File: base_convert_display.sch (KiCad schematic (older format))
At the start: 49 parts, among them Q10 Q_PNP_BEC, Q11 Q_NPN_BEC, Q12 Q_NPN_BEC, Q13 Q_NPN_BEC, Q14 Q_NPN_BEC, Q15 Q_NPN_BEC, Q16 Q_NPN_BEC, Q17 Q_NPN_BEC, Q2 Q_PNP_BEC, Q26 Q_PNP_BEC, Q27 Q_NPN_BEC, Q3 Q_PNP_BEC, Q4 Q_PNP_BEC, Q5 Q_PNP_BEC, Q6 Q_PNP_BEC, Q7 Q_PNP_BEC, Q8 Q_PNP_BEC, Q9 Q_PNP_BEC

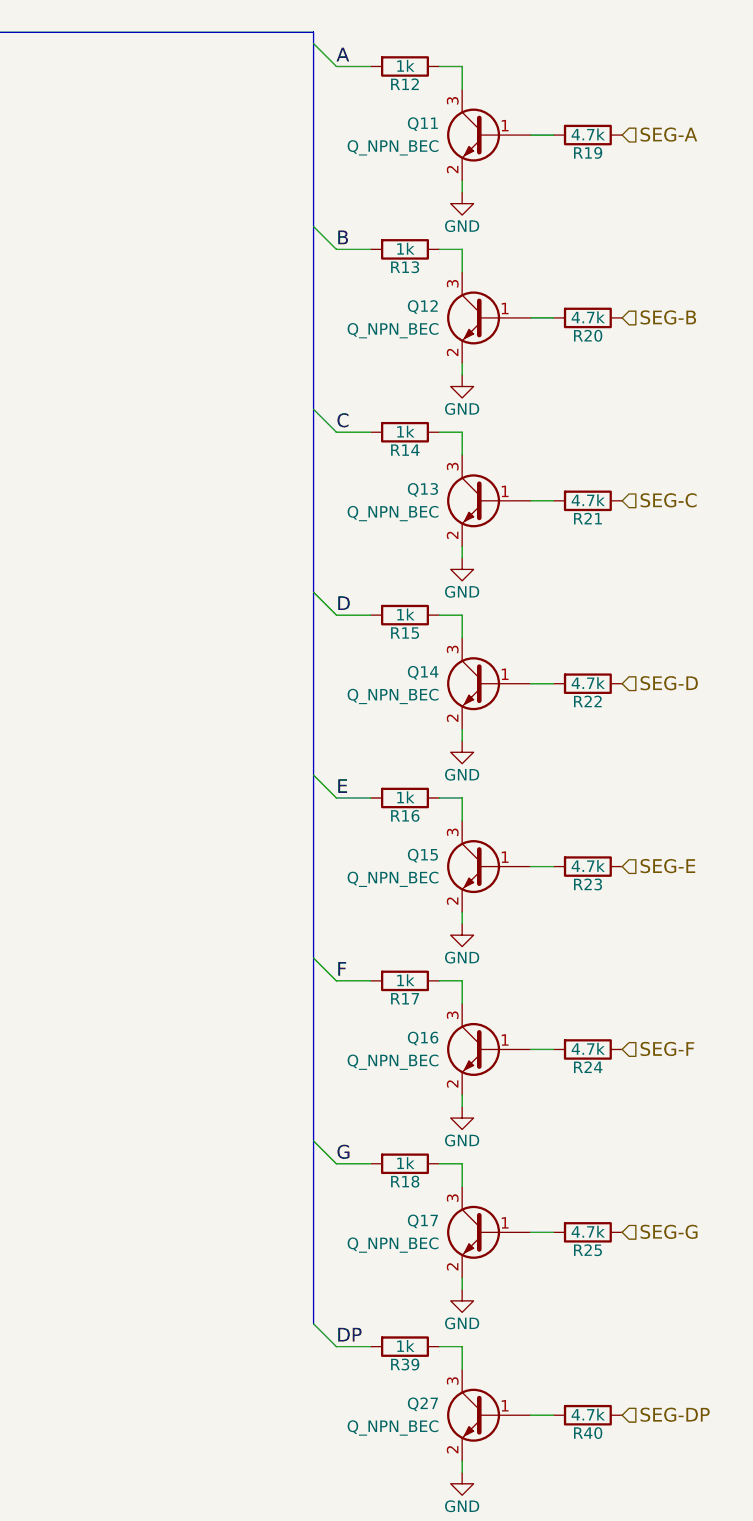
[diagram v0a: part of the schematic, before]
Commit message: change led current limit resistor value
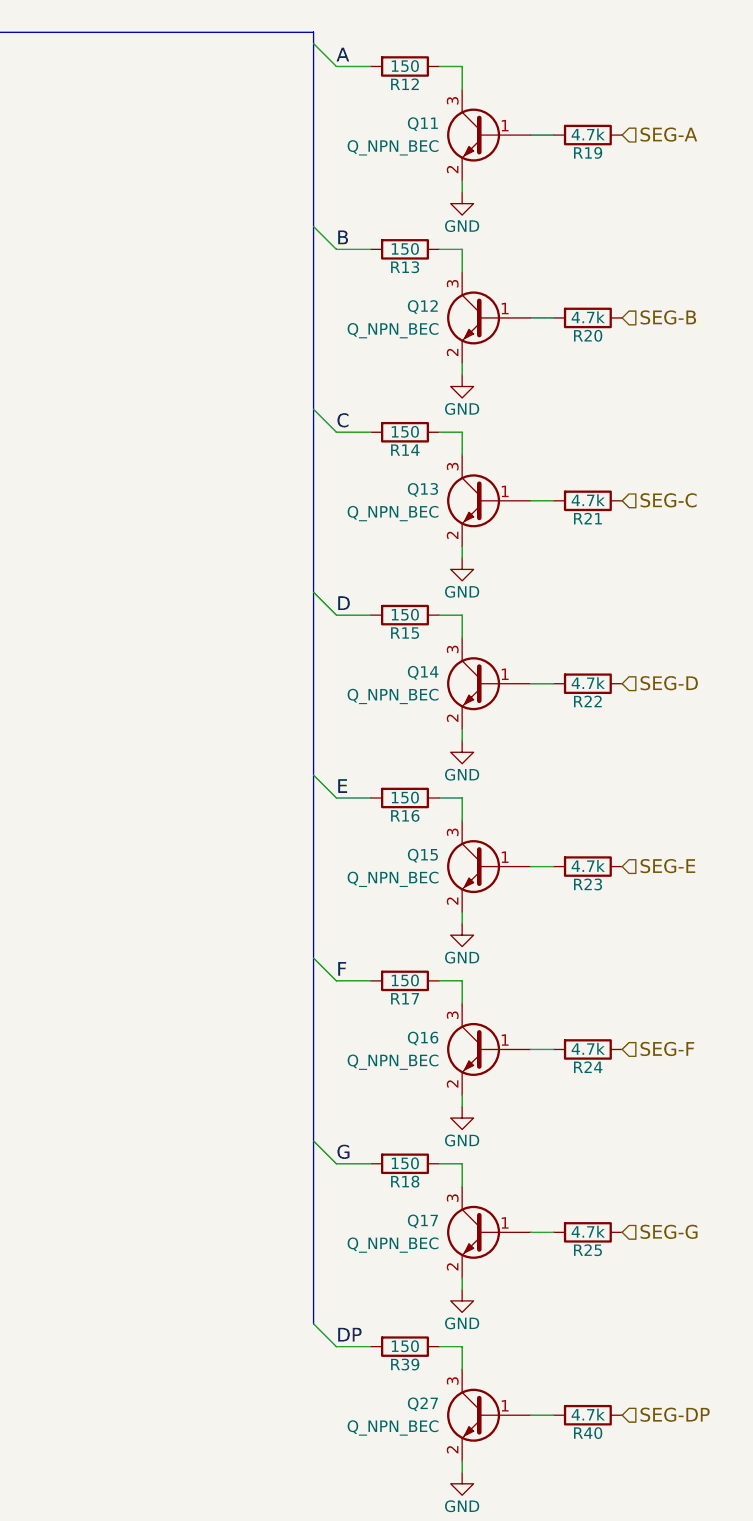
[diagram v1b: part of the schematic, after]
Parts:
- R12, R13, R14, R15, R16, R17, R18, R39: value 1k -> 150; Description (none) -> NONE; Manufacture (none) -> NONE; Mfg Part Number (none) -> NONE; Package (none) -> NONE
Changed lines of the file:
@@
 P 8750 700
 F 0 "R12" V 8830 700 50  0000 C CNN
-F 1 "1k" V 8750 700 50  0000 C CNN
+F 1 "150" V 8750 700 50  0000 C CNN
 F 2 "Resistors_SMD:R_0603" V 8680 700 50  0001 C CNN
 F 3 "" H 8750 700 50  0001 C CNN
+F 4 "NONE" H 8750 700 60  0001 C CNN "Manufacture"
+F 5 "NONE" H 8750 700 60  0001 C CNN "Mfg Part Number"
+F 6 "NONE" H 8750 700 60  0001 C CNN "Package"
+F 7 "NONE" H 8750 700 60  0001 C CNN "Description"
 	1    8750 700
 	0    1    1    0
@@
 P 8750 1500
 F 0 "R13" V 8830 1500 50  0000 C CNN
-F 1 "1k" V 8750 1500 50  0000 C CNN
+F 1 "150" V 8750 1500 50  0000 C CNN
 F 2 "Resistors_SMD:R_0603" V 8680 1500 50  0001 C CNN
 F 3 "" H 8750 1500 50  0001 C CNN
+F 4 "NONE" H 8750 1500 60  0001 C CNN "Manufacture"
+F 5 "NONE" H 8750 1500 60  0001 C CNN "Mfg Part Number"
+F 6 "NONE" H 8750 1500 60  0001 C CNN "Package"
+F 7 "NONE" H 8750 1500 60  0001 C CNN "Description"
 	1    8750 1500
 	0    1    1    0
@@
 P 8750 2300
 F 0 "R14" V 8830 2300 50  0000 C CNN
-F 1 "1k" V 8750 2300 50  0000 C CNN
+F 1 "150" V 8750 2300 50  0000 C CNN
 F 2 "Resistors_SMD:R_0603" V 8680 2300 50  0001 C CNN
 F 3 "" H 8750 2300 50  0001 C CNN
+F 4 "NONE" H 8750 2300 60  0001 C CNN "Manufacture"
+F 5 "NONE" H 8750 2300 60  0001 C CNN "Mfg Part Number"
+F 6 "NONE" H 8750 2300 60  0001 C CNN "Package"
+F 7 "NONE" H 8750 2300 60  0001 C CNN "Description"
 	1    8750 2300
 	0    1    1    0
@@
 P 8750 3100
 F 0 "R15" V 8830 3100 50  0000 C CNN
-F 1 "1k" V 8750 3100 50  0000 C CNN
+F 1 "150" V 8750 3100 50  0000 C CNN
 F 2 "Resistors_SMD:R_0603" V 8680 3100 50  0001 C CNN
 F 3 "" H 8750 3100 50  0001 C CNN
+F 4 "NONE" H 8750 3100 60  0001 C CNN "Manufacture"
+F 5 "NONE" H 8750 3100 60  0001 C CNN "Mfg Part Number"
+F 6 "NONE" H 8750 3100 60  0001 C CNN "Package"
+F 7 "NONE" H 8750 3100 60  0001 C CNN "Description"
 	1    8750 3100
 	0    1    1    0
@@
 P 8750 3900
 F 0 "R16" V 8830 3900 50  0000 C CNN
-F 1 "1k" V 8750 3900 50  0000 C CNN
+F 1 "150" V 8750 3900 50  0000 C CNN
 F 2 "Resistors_SMD:R_0603" V 8680 3900 50  0001 C CNN
 F 3 "" H 8750 3900 50  0001 C CNN
+F 4 "NONE" H 8750 3900 60  0001 C CNN "Manufacture"
+F 5 "NONE" H 8750 3900 60  0001 C CNN "Mfg Part Number"
+F 6 "NONE" H 8750 3900 60  0001 C CNN "Package"
+F 7 "NONE" H 8750 3900 60  0001 C CNN "Description"
 	1    8750 3900
 	0    1    1    0
@@
 P 8750 4700
 F 0 "R17" V 8830 4700 50  0000 C CNN
-F 1 "1k" V 8750 4700 50  0000 C CNN
+F 1 "150" V 8750 4700 50  0000 C CNN
 F 2 "Resistors_SMD:R_0603" V 8680 4700 50  0001 C CNN
 F 3 "" H 8750 4700 50  0001 C CNN
+F 4 "NONE" H 8750 4700 60  0001 C CNN "Manufacture"
+F 5 "NONE" H 8750 4700 60  0001 C CNN "Mfg Part Number"
+F 6 "NONE" H 8750 4700 60  0001 C CNN "Package"
+F 7 "NONE" H 8750 4700 60  0001 C CNN "Description"
 	1    8750 4700
 	0    1    1    0
@@
 P 8750 5500
 F 0 "R18" V 8830 5500 50  0000 C CNN
-F 1 "1k" V 8750 5500 50  0000 C CNN
+F 1 "150" V 8750 5500 50  0000 C CNN
 F 2 "Resistors_SMD:R_0603" V 8680 5500 50  0001 C CNN
 F 3 "" H 8750 5500 50  0001 C CNN
+F 4 "NONE" H 8750 5500 60  0001 C CNN "Manufacture"
+F 5 "NONE" H 8750 5500 60  0001 C CNN "Mfg Part Number"
+F 6 "NONE" H 8750 5500 60  0001 C CNN "Package"
+F 7 "NONE" H 8750 5500 60  0001 C CNN "Description"
 	1    8750 5500
 	0    1    1    0
@@
 P 8750 6300
 F 0 "R39" V 8830 6300 50  0000 C CNN
-F 1 "1k" V 8750 6300 50  0000 C CNN
+F 1 "150" V 8750 6300 50  0000 C CNN
 F 2 "Resistors_SMD:R_0603" V 8680 6300 50  0001 C CNN
 F 3 "" H 8750 6300 50  0001 C CNN
+F 4 "NONE" H 8750 6300 60  0001 C CNN "Manufacture"
+F 5 "NONE" H 8750 6300 60  0001 C CNN "Mfg Part Number"
+F 6 "NONE" H 8750 6300 60  0001 C CNN "Package"
+F 7 "NONE" H 8750 6300 60  0001 C CNN "Description"
 	1    8750 6300
 	0    1    1    0

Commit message: update switch fields
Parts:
- DS1:  H 6100 650 50 0001 C CNN  10-DIP (0.400 -> (none); Description (none) -> LED 7-SEG .40\" 2DGT SUPER RED CA; Package (none) -> 10-DIP
- DS2:  H 6100 1700 50 0001 C CNN  10-DIP (0.400 -> (none); Description (none) -> LED 7-SEG .40\" 2DGT SUPER RED CA; Package (none) -> 10-DIP
- DS3:  H 6100 2850 50 0001 C CNN  10-DIP (0.400 -> (none); Description (none) -> LED 7-SEG .40\" 2DGT SUPER RED CA; Package (none) -> 10-DIP
- DS4:  H 6100 3900 50 0001 C CNN  10-DIP (0.400 -> (none); Description (none) -> LED 7-SEG .40\" 2DGT SUPER RED CA; Package (none) -> 10-DIP
- DS5:  H 6100 4950 50 0001 C CNN  10-DIP (0.400 -> (none); Description (none) -> LED 7-SEG .40\" 2DGT SUPER RED CA; Package (none) -> 10-DIP
- R12, R13, R14, R15, R16, R17, R18, R39: Description NONE -> (none); Manufacture NONE -> (none); Mfg Part Number NONE -> (none); Package NONE -> (none)

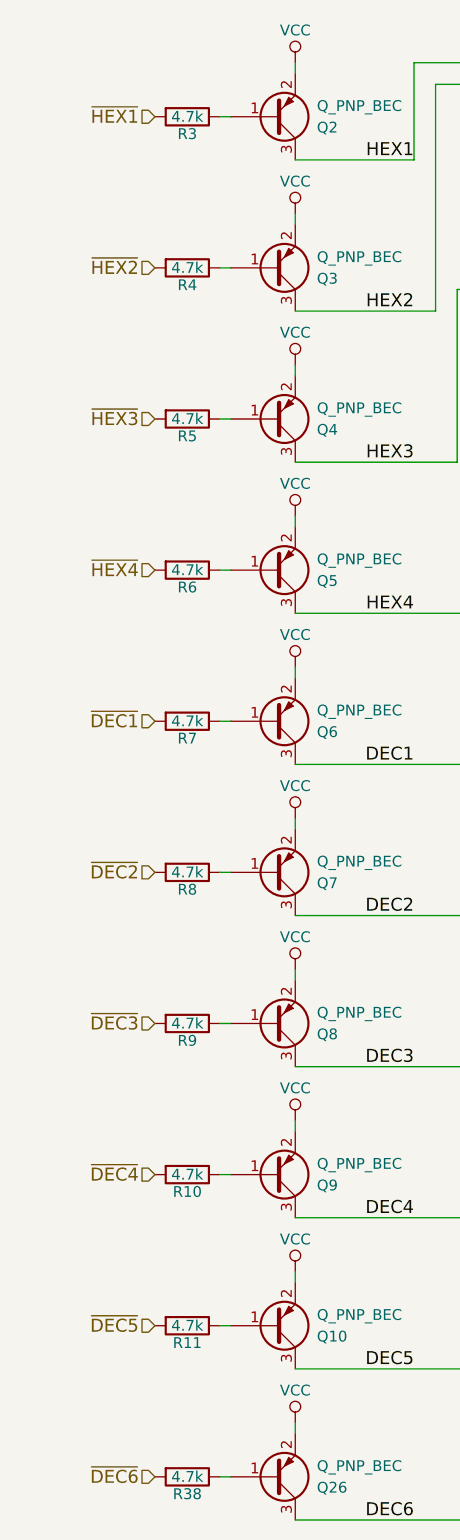
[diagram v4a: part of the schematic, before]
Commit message: renamed digit control lines
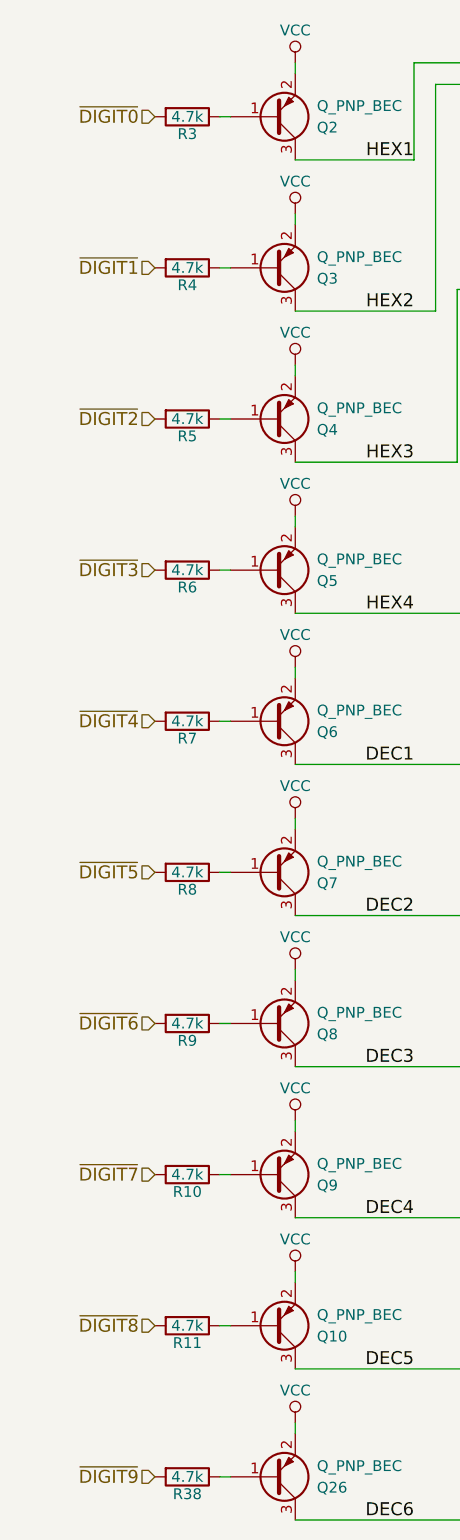
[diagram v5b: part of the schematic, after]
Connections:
- net ~DEC1 renamed ~DIGIT4
- net ~DEC2 renamed ~DIGIT5
- net ~DEC3 renamed ~DIGIT6
- net ~DEC4 renamed ~DIGIT7
- net ~DEC5 renamed ~DIGIT8
- net ~DEC6 renamed ~DIGIT9
- net ~HEX1 renamed ~DIGIT0
- net ~HEX2 renamed ~DIGIT1
- net ~HEX3 renamed ~DIGIT2
- net ~HEX4 renamed ~DIGIT3
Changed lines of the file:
@@
 Text Label 4100 1850 0    60   ~ 0
-HEX4
-Text Label 2300 1150 2    60   ~ 0
-HEX1
-Text Label 2300 1850 2    60   ~ 0
-HEX2
-Text Label 2300 2550 2    60   ~ 0
-HEX3
-Text Label 2300 3250 2    60   ~ 0
 HEX4
 Text Label 4100 2900 0    60   ~ 0
@@
 G
 Text HLabel 1100 950  0    60   Input ~ 0
-~HEX1
-Text HLabel 1100 1650 0    60   Input ~ 0
-~HEX2
-Text HLabel 1100 2350 0    60   Input ~ 0
-~HEX3
-Text HLabel 1100 3050 0    60   Input ~ 0
-~HEX4
-Text HLabel 1100 3750 0    60   Input ~ 0
-~DEC1
-Text HLabel 1100 4450 0    60   Input ~ 0
-~DEC2
-Text HLabel 1100 5150 0    60   Input ~ 0
-~DEC3
-Text HLabel 1100 5850 0    60   Input ~ 0
-~DEC4
-Text HLabel 1100 6550 0    60   Input ~ 0
-~DEC5
+~DIGIT0
 Text HLabel 9700 1000 2    60   Input ~ 0
 SEG-A
@@
 Text Label 2300 7450 2    60   ~ 0
 DEC6
-Text HLabel 1100 7250 0    60   Input ~ 0
-~DEC6
 Text Label 4100 5100 0    60   ~ 0
 DEC6
@@
 Entry Wire Line
 	8350 6200 8450 6300
+Text HLabel 1100 1650 0    60   Input ~ 0
+~DIGIT1
+Text HLabel 1100 2350 0    60   Input ~ 0
+~DIGIT2
+Text HLabel 1100 3050 0    60   Input ~ 0
+~DIGIT3
+Text HLabel 1100 3750 0    60   Input ~ 0
+~DIGIT4
+Text HLabel 1100 4450 0    60   Input ~ 0
+~DIGIT5
+Text HLabel 1100 5150 0    60   Input ~ 0
+~DIGIT6
+Text HLabel 1100 5850 0    60   Input ~ 0
+~DIGIT7
+Text HLabel 1100 6550 0    60   Input ~ 0
+~DIGIT8
+Text HLabel 1100 7250 0    60   Input ~ 0
+~DIGIT9
+Text Label 2300 3250 2    60   ~ 0
+HEX4
+Text Label 2300 2550 2    60   ~ 0
+HEX3
+Text Label 2300 1850 2    60   ~ 0
+HEX2
+Text Label 2300 1150 2    60   ~ 0
+HEX1
 $EndSCHEMATC
